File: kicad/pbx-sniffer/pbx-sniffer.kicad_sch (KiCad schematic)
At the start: 6 parts, among them U1 STM32H7R3V8Tx, U4 MX25L3233FM2

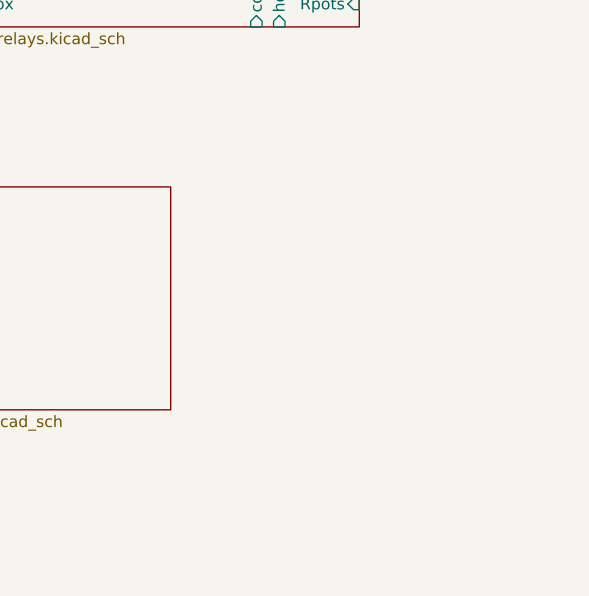
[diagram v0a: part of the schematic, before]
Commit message: added adc sheet
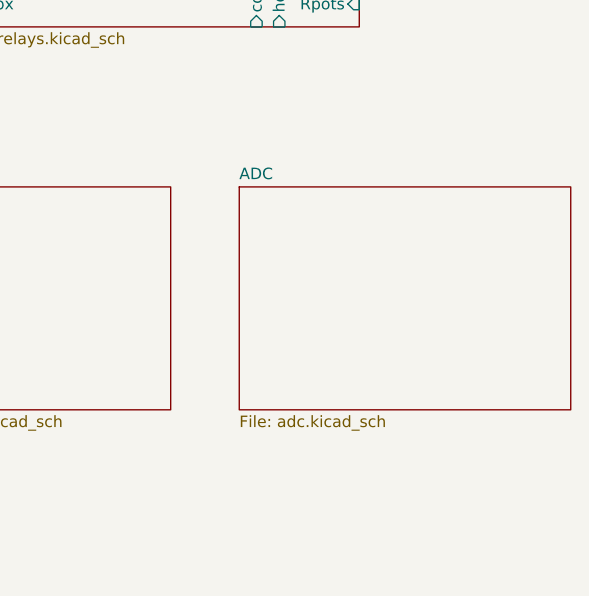
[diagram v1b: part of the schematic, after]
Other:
- added sheet ADC (adc.kicad_sch)

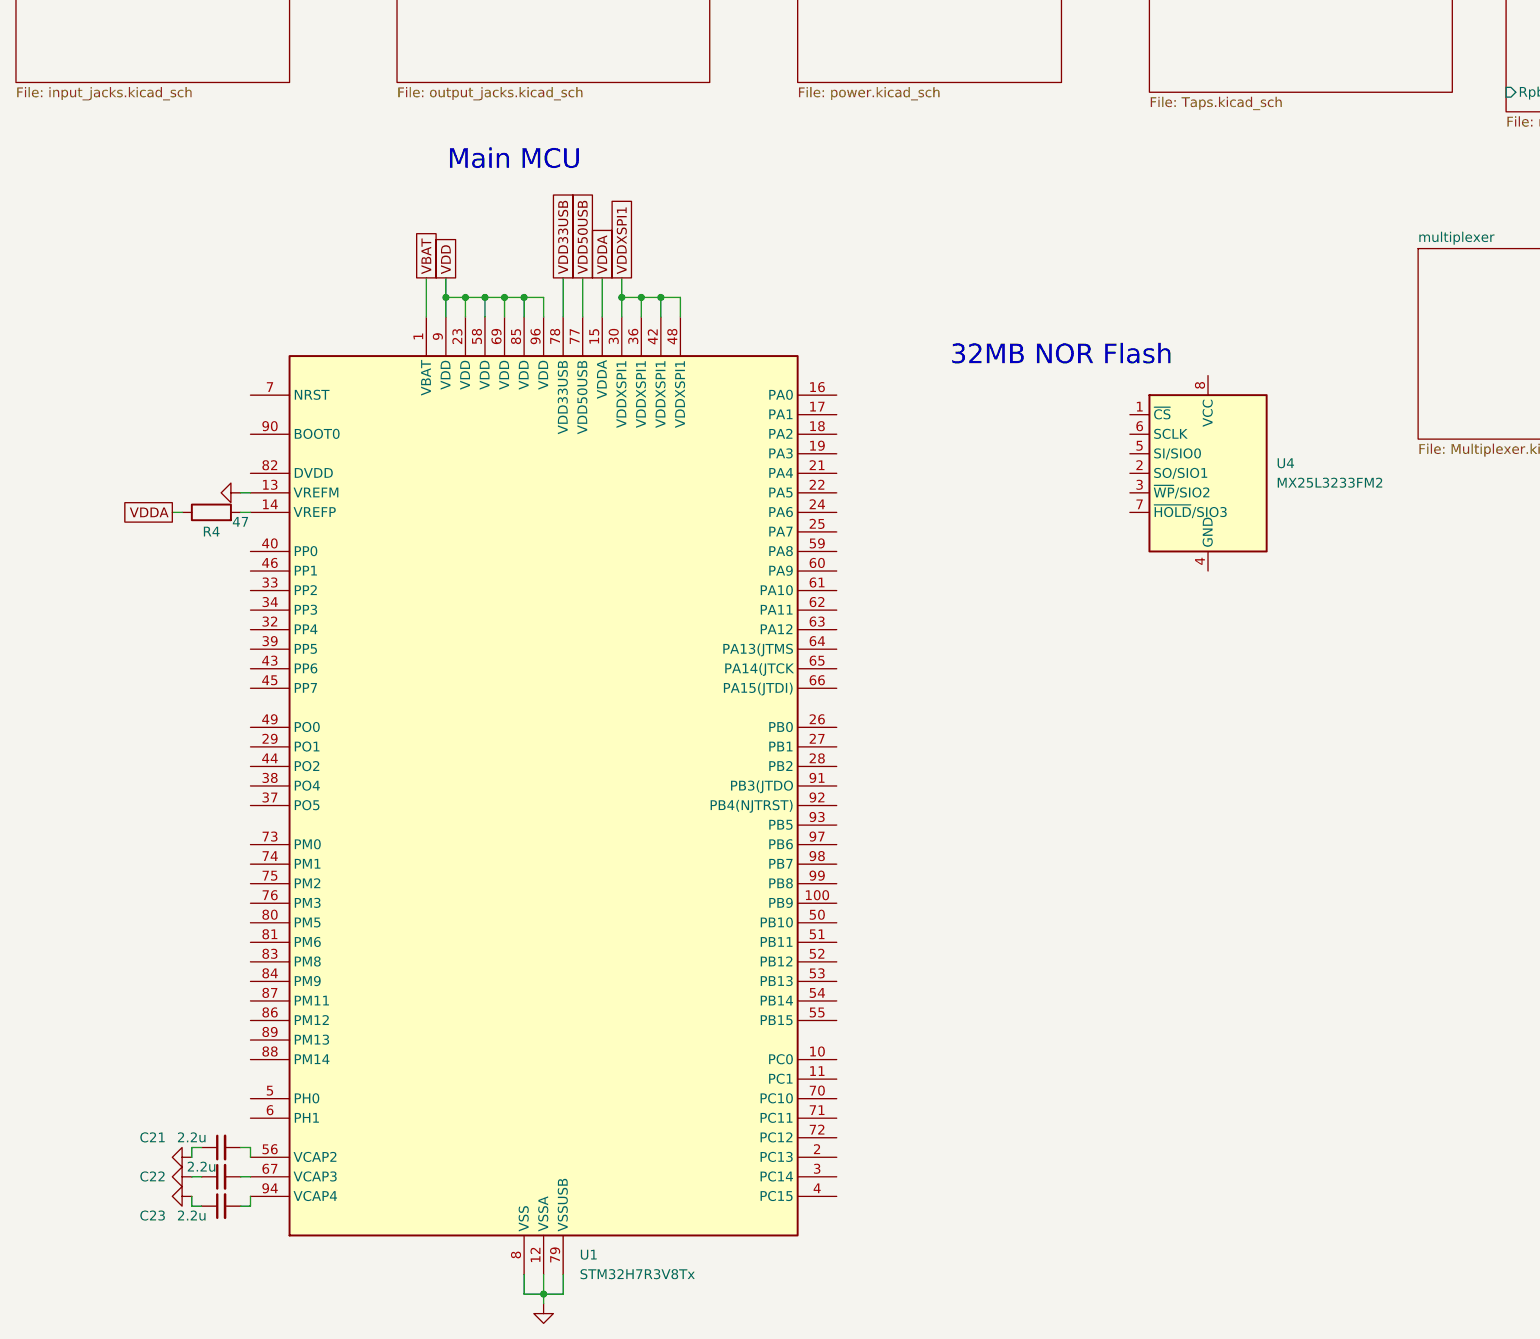
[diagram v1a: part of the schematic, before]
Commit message: remove MCU and add symbols for stm32 nucleo morpho connectors
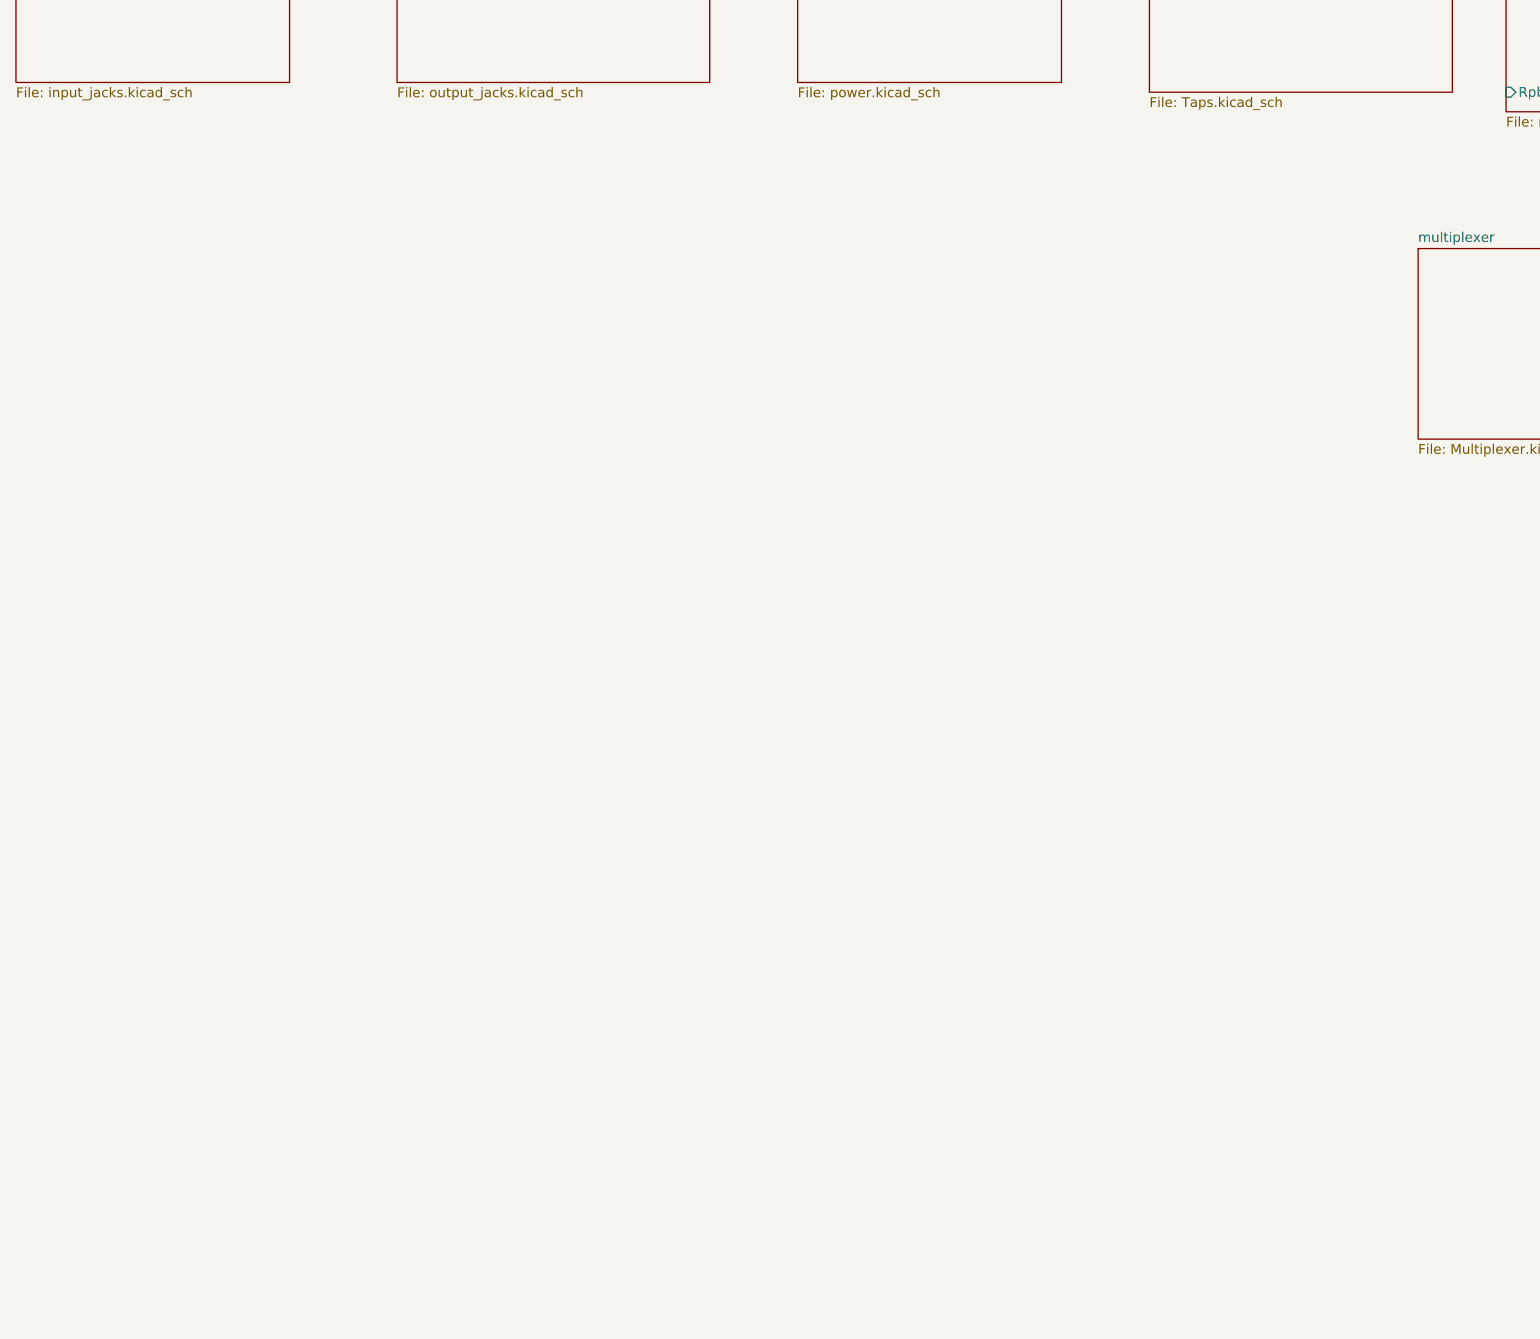
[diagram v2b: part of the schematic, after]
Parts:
- removed C21, C22, C23: 2.2u, symbol Device:C_Small
- removed R4: 47, symbol Device:R
- removed U1: STM32H7R3V8Tx, Package_QFP:LQFP-100_14x14mm_P0.5mm, symbol MCU_ST_STM32H7:STM32H7R3V8Tx
- removed U4: MX25L3233FM2, Package_SO:SOIC-8_5.3x5.3mm_P1.27mm, symbol Memory_Flash:MX25L3233FM2
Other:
- note removed: "32MB NOR Flash"
- note removed: "Main MCU"

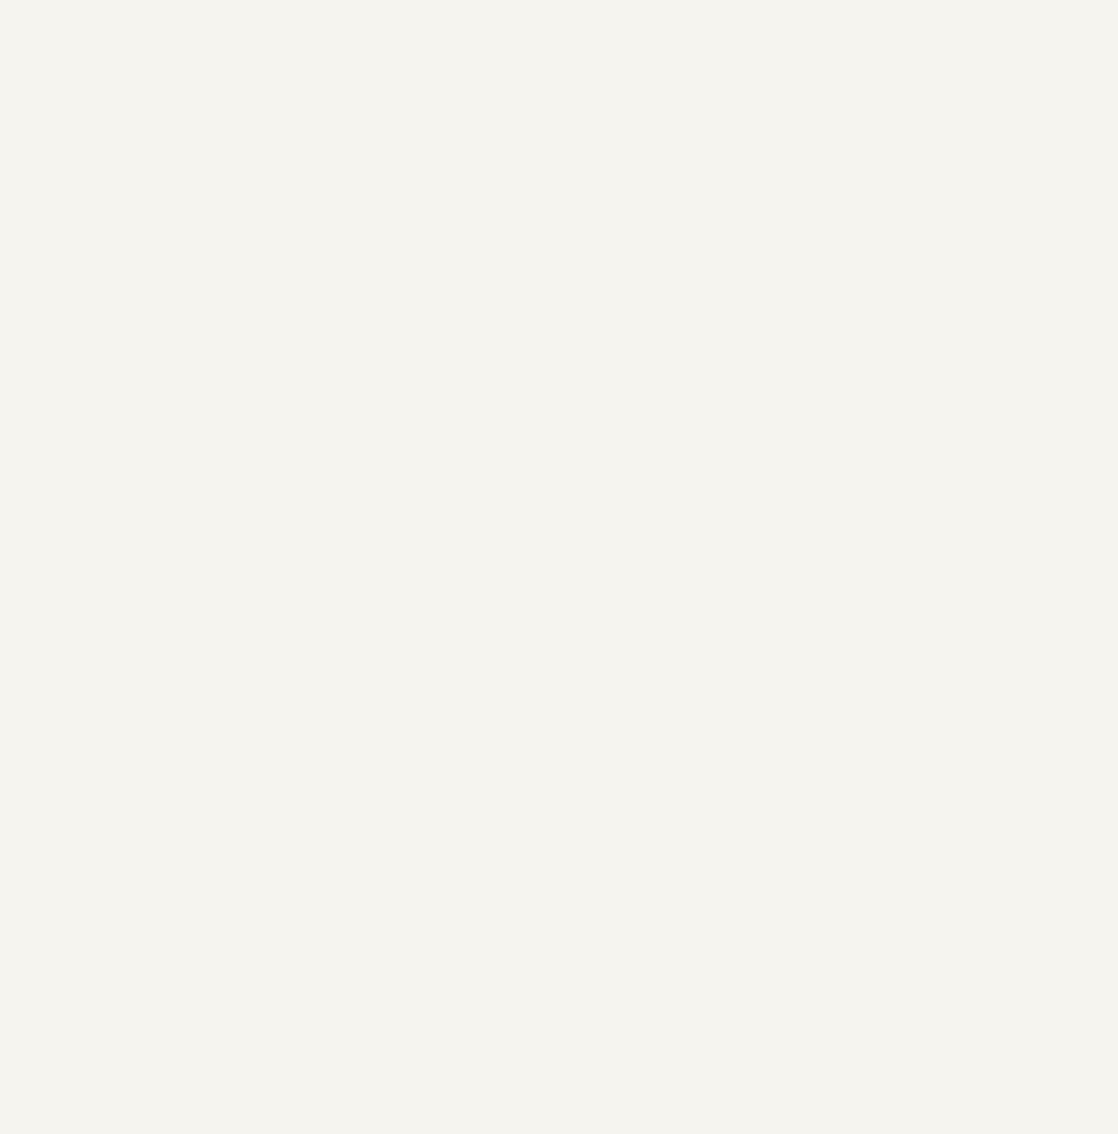
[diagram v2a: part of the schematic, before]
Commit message: update the symbols for the nucleo pins
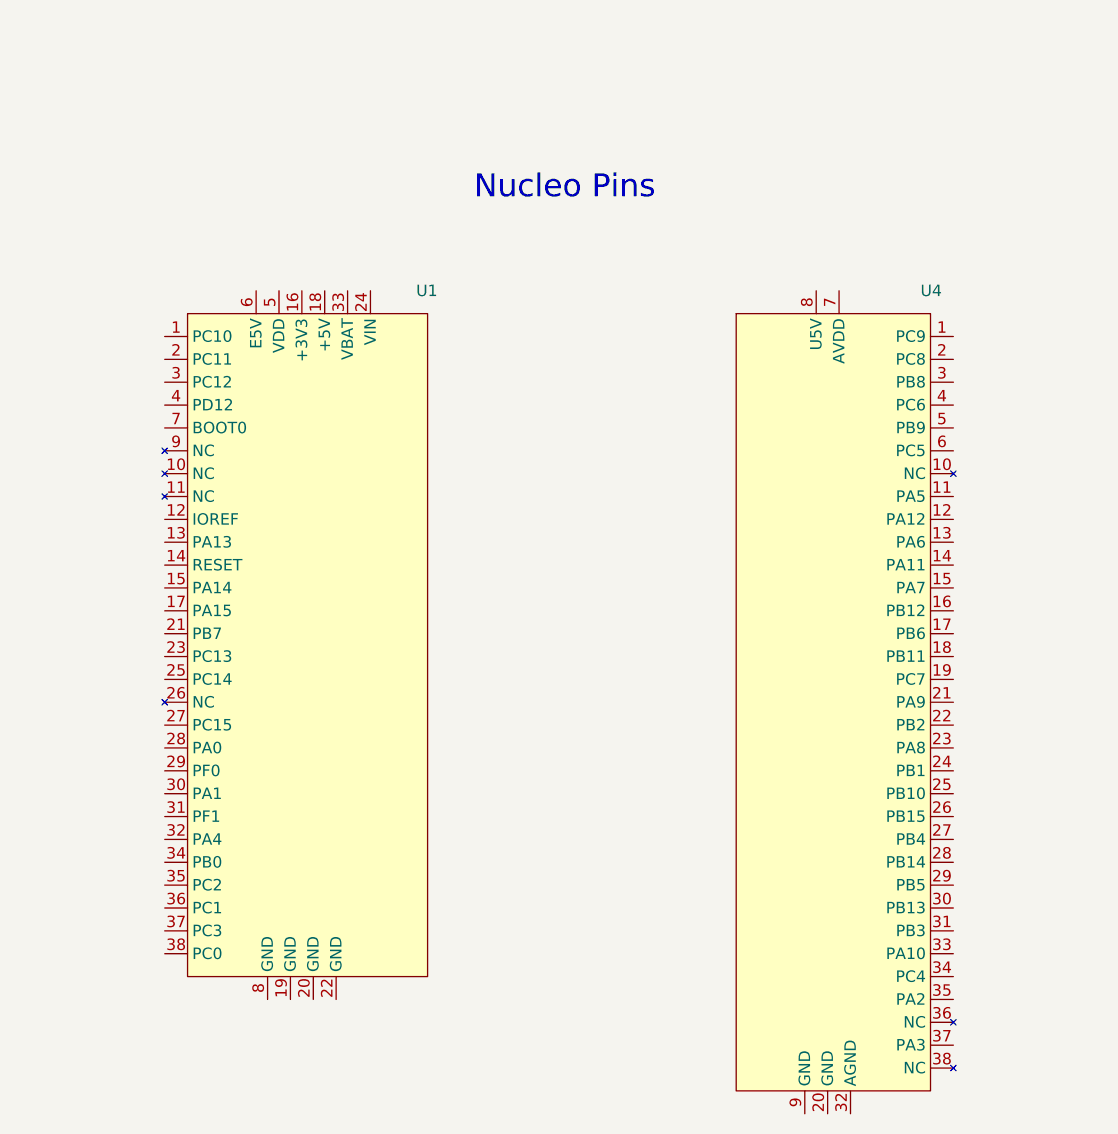
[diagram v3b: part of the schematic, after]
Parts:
- added U1: ~, Connector_PinHeader_2.54mm:PinHeader_2x19_P2.54mm_Vertical, symbol Phones:STM32NucleoF303RE_CN7
- added U4: ~, Connector_PinHeader_2.54mm:PinHeader_2x19_P2.54mm_Vertical, symbol Phones:STM32NucleoF303RE_CN10
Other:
- note added: "Nucleo Pins"

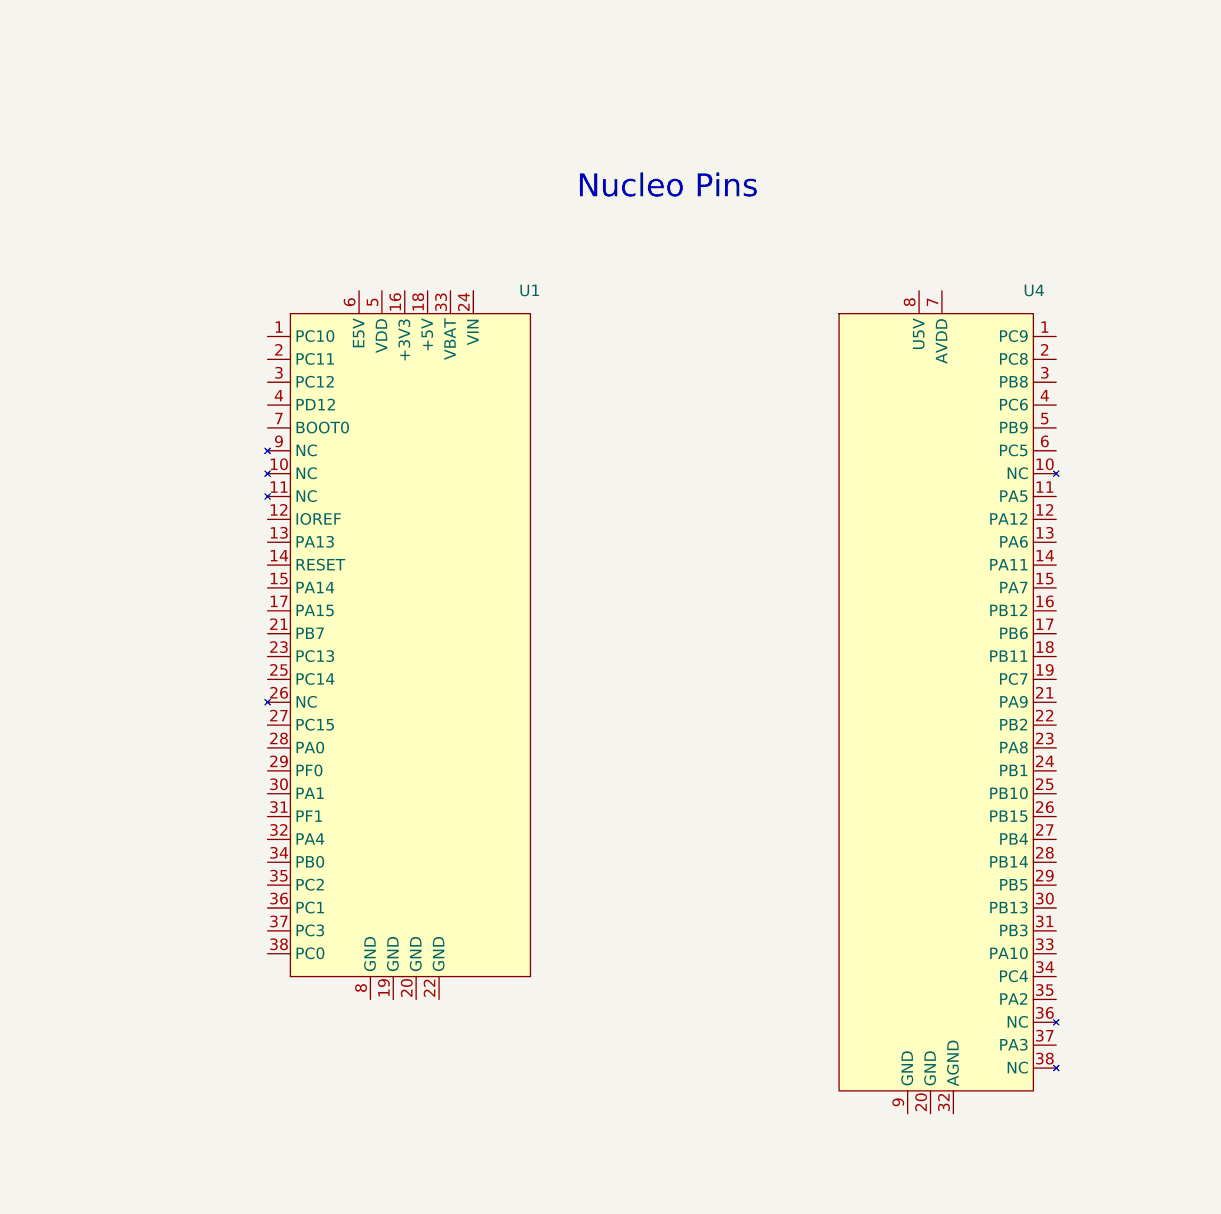
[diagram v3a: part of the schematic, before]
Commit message: make nucleo pins a shared symbol with units
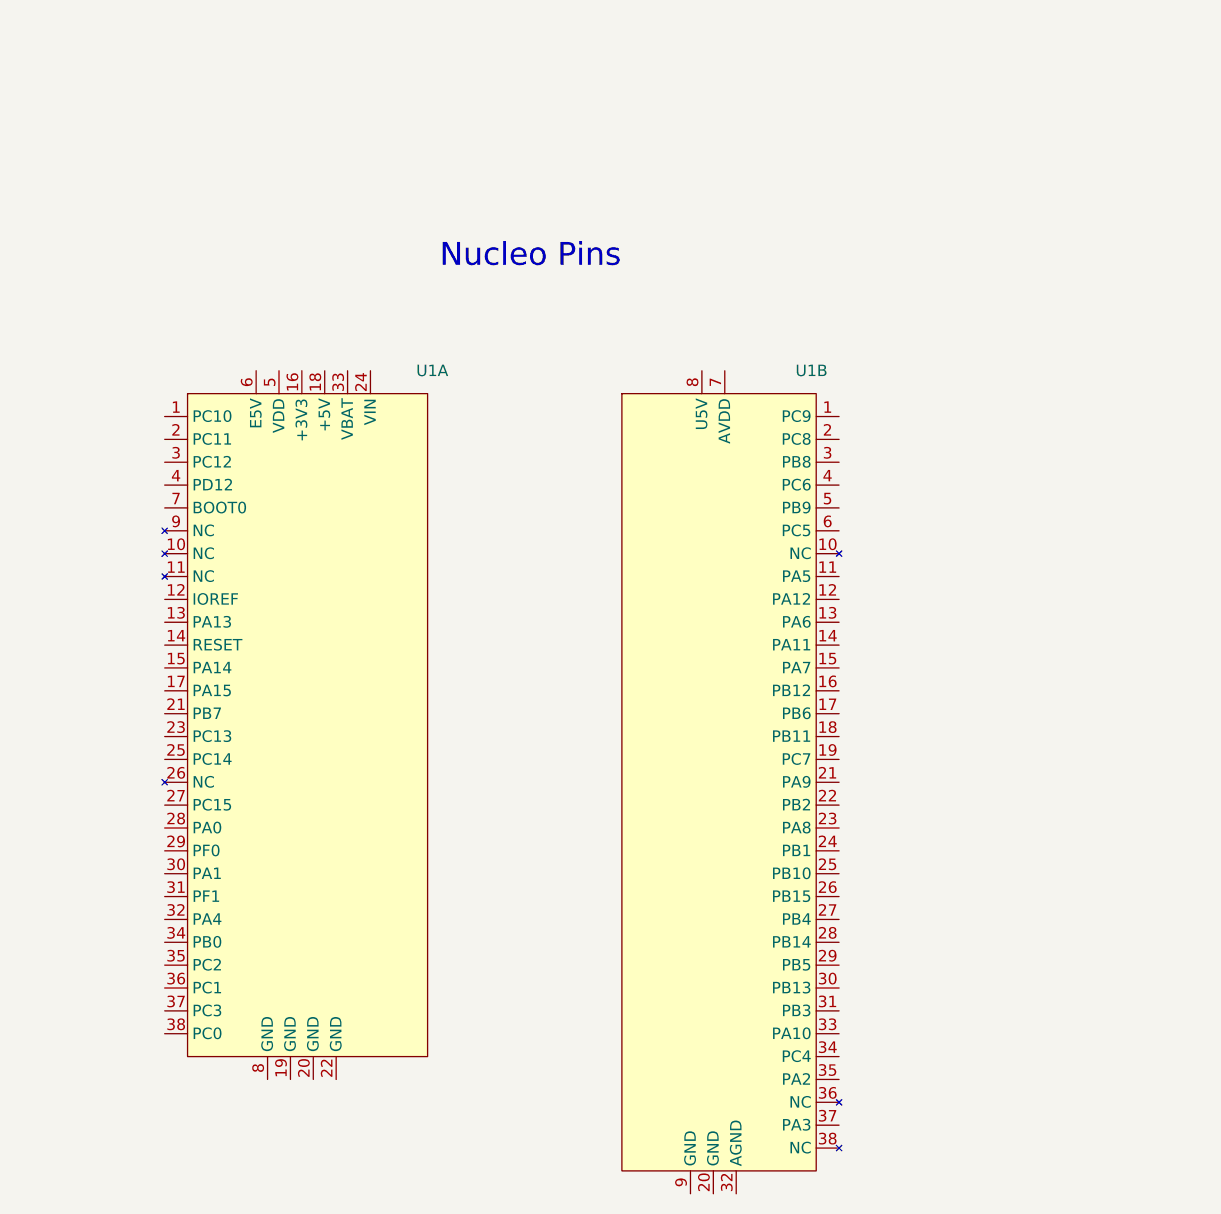
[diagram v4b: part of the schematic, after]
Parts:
- removed U1: ~, Connector_PinHeader_2.54mm:PinHeader_2x19_P2.54mm_Vertical, symbol Phones:STM32NucleoF303RE_CN7
- removed U4: ~, Connector_PinHeader_2.54mm:PinHeader_2x19_P2.54mm_Vertical, symbol Phones:STM32NucleoF303RE_CN10
- added U1: ~, Connector_PinHeader_2.54mm:PinHeader_2x19_P2.54mm_Vertical, symbol Phones:STM32NucleoF303RE
